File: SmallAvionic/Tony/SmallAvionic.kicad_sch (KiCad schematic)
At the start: 107 parts, among them J1 Boot_mode_pin, J10 Conn_01x04, J12 Conn_01x04, J2 USB_C_Receptacle_USB2.0_16P, J3 Conn_01x04, J4 Conn_01x03, J5 Conn_01x02, J6 Screw_Terminal_01x01, Q1 TSM3481CX6 RFG, Q2 TSM3481CX6 RFG, Q5 NMOS, SW1 SW_Push, SW2 USER_Buttom, U1 STM32F103C8Tx, U2 LD1117S33TR_SOT223, U3 LTC4412xS6, U4 TPS54538RQFR, U5 BMI088, U6 BMP390, U7 MMC5983MA, U8 W25Q128JVS, Y1 8Mhz

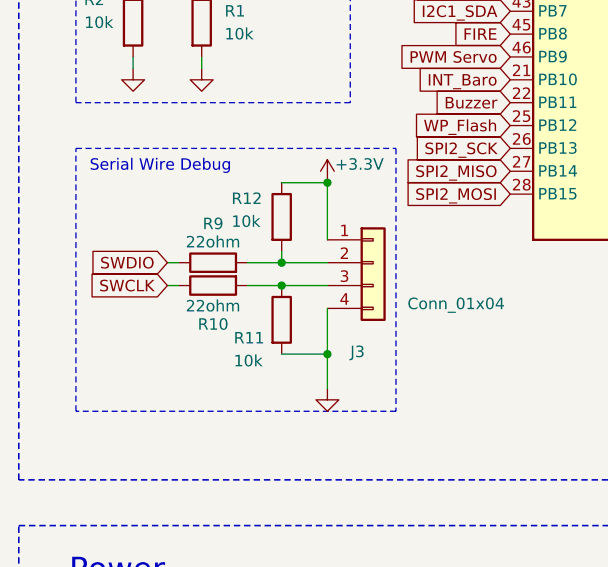
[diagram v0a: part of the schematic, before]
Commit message: finished sensors except gps
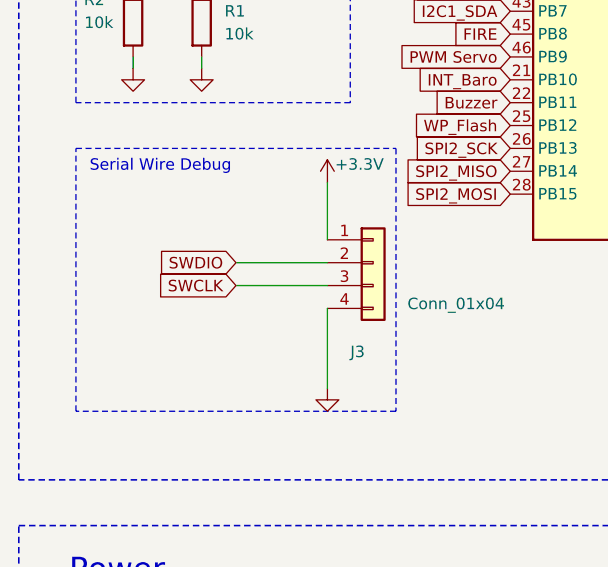
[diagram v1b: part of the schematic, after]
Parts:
- removed R10, R9: 22ohm, symbol Device:R
- removed R11, R12: 10k, symbol Device:R
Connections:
- net SWCLK: now also J3.3 (Pin_3)
- net SWDIO: now also J3.2 (Pin_2)
